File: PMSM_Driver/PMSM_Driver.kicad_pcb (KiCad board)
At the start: 4 copper layers, 244.8 x 144.1 mm, 234 parts, among them J1 1714984, J10 AFBR-2624Z, J11 AFBR-2624Z, J12 AFBR-2624Z, J13 AFBR-2624Z, J14 AFBR-2624Z, J15 AFBR-2624Z, J16 AFBR-2624Z, J17 AFBR-1624Z, J18 AFBR-1624Z, J2 AFBR-2624Z, J3 1714971, J4 1714971, J5 AFBR-1624Z, J6 AFBR-2624Z, J7 AFBR-2624Z, J8 AFBR-2624Z, J9 AFBR-2624Z, Q1 BC846, Q10 BC846, Q11 RGCL60TK60, Q12 RGCL60TK60, Q13 RGCL60TK60, Q14 RGCL60TK60, Q15 BC846, Q16 RGCL60TK60, Q17 RGCL60TK60, Q18 RGCL60TK60, Q19 RGCL60TK60, Q2 BC846, Q20 BC846, Q21 BC846, Q22 BC846, Q23 BC846, Q24 BC846, Q3 BC846, Q4 BC846, Q5 RGCL60TK60, Q6 RGCL60TK60, Q7 RGCL60TK60, Q8 RGCL60TK60, Q9 BC846, U1 74LVC1G04, U10 HCPL-3120, U11 HCPL-3120, U12 HCPL-3120, U13 74LVC1G04, U14 74LVC1G04, U15 74LVC1G04, U16 MGJ2D051515SC, U17 MGJ2D051515SC, U18 MGJ2D051515SC, U19 HCPL-3120, U2 MGJ2D051515SC, U20 HCPL-3120, U21 HCPL-3120, U22 74LVC1G04, U23 74LVC1G04, U24 74LVC1G04, U25 MGJ2D051515SC, U26 MGJ2D051515SC, U27 MGJ2D051515SC, U28 HCPL-3120, U29 HCPL-3120, U3 HCPL-3120, U30 HCPL-3120, U31 74LVC1G04, U32 74LVC1G04, U33 MGJ2D051515SC, U34 MGJ2D051515SC, U35 HCPL-3120, U36 HCPL-3120, U37 VS-E5TH3006S2L-M3, U38 VS-E5TH3006S2L-M3, U39 VS-E5TH3006S2L-M3, U4 74LVC1G04, U40 VS-E5TH3006S2L-M3, U41 VS-E5TH3006S2L-M3, U42 VS-E5TH3006S2L-M3, U43 VS-E5TH3006S2L-M3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

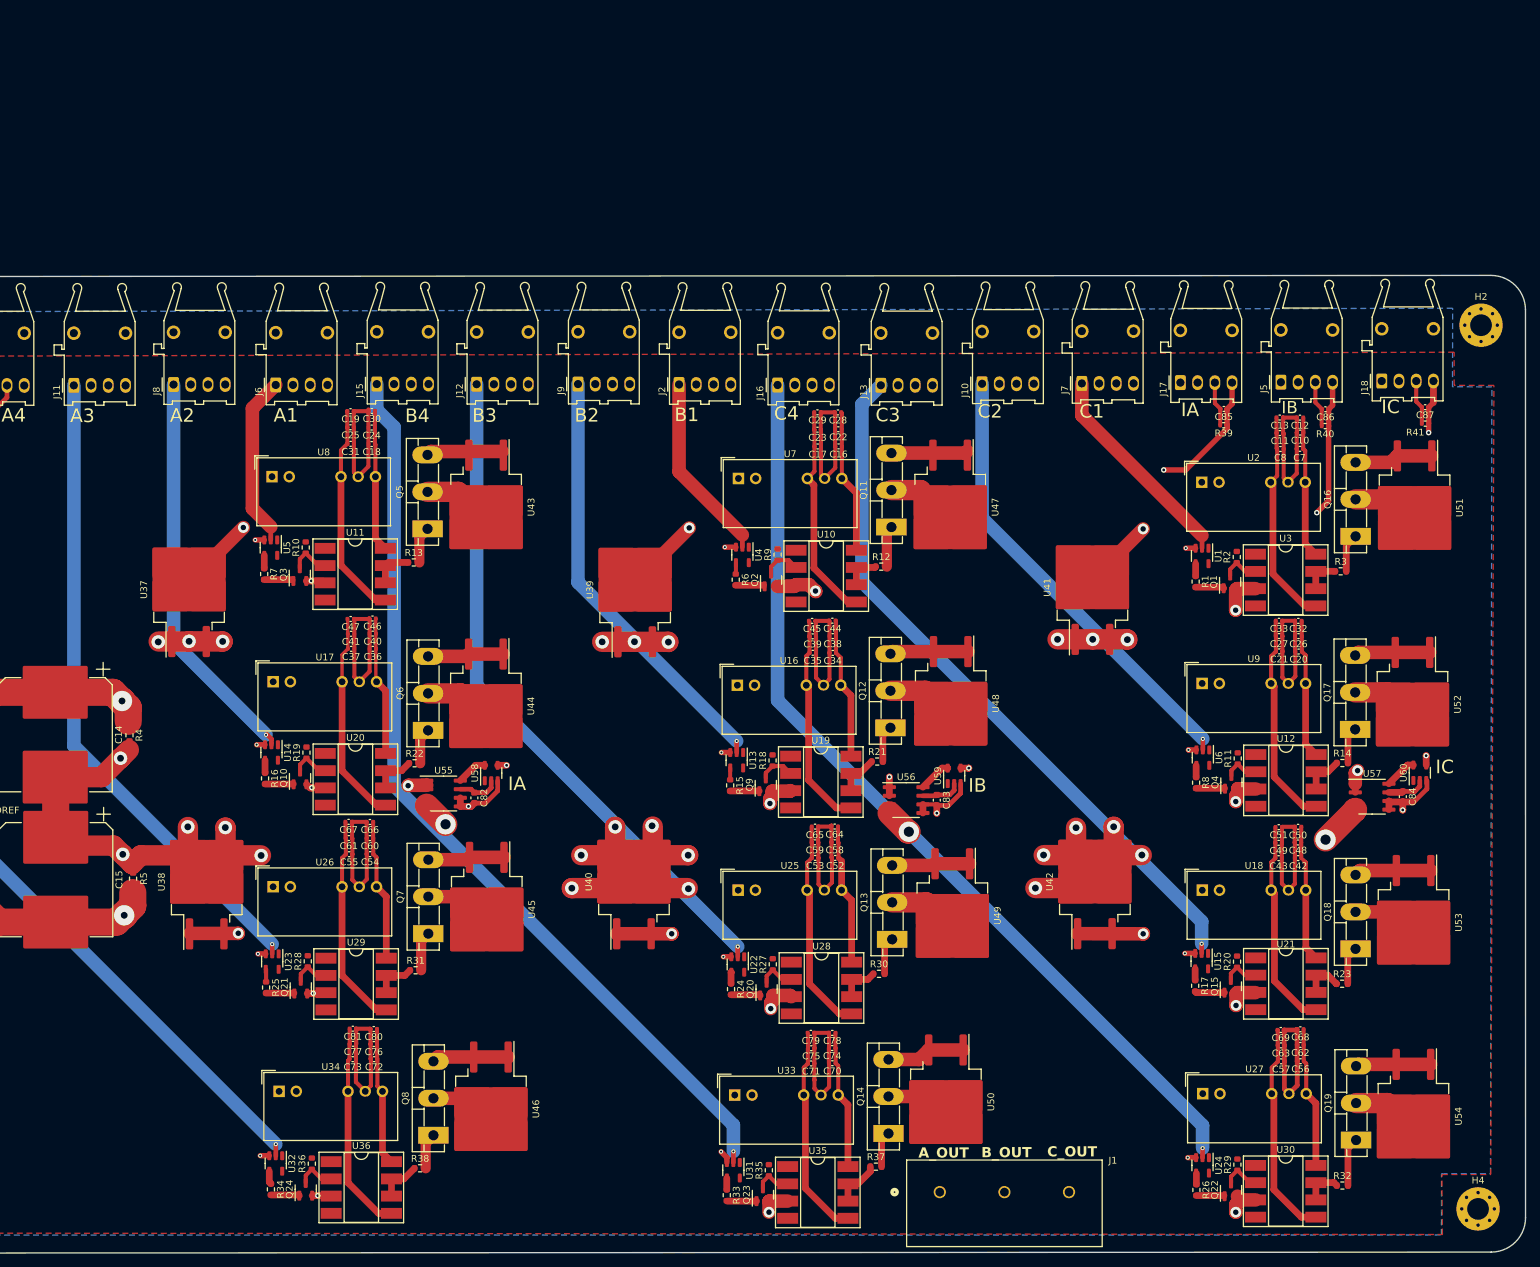
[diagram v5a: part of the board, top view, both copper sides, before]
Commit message: updated PCB layout: gate drive protection
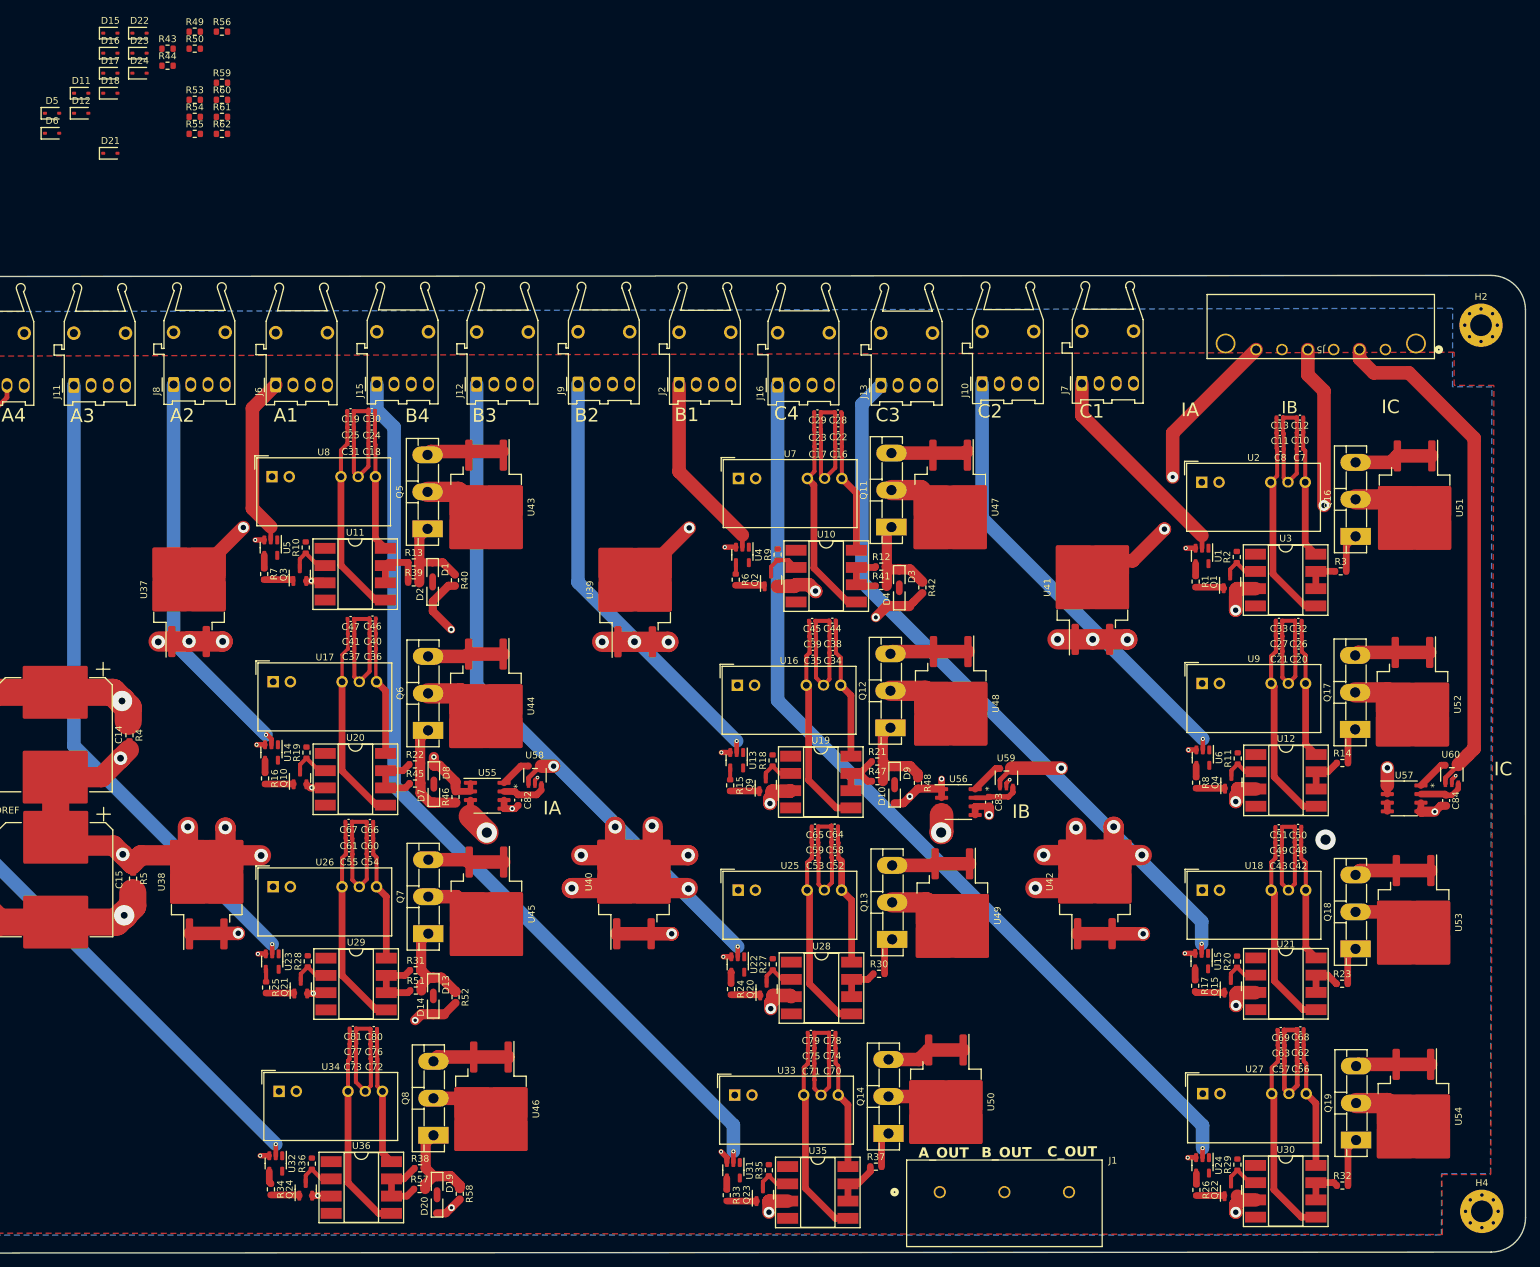
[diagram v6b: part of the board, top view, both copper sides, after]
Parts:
- removed C85, C86, C87: 0.1u, Capacitor_SMD:C_0402_1005Metric
- removed J17, J18: AFBR-1624Z, OptoDevice:Broadcom_AFBR-16xxZ_Horizontal
- added D1: BZX384C18, Diode_SMD:D_SOD-323, F.Cu at (135.7, 81.1)
- added D10: BZX384C18, Diode_SMD:D_SOD-323, F.Cu at (203.8, 114.5)
- added D11: BZX384C18, Diode_SMD:D_SOD-323, F.Cu at (83.9, 11.0)
- added D12: BZX384C18, Diode_SMD:D_SOD-323, F.Cu at (83.9, 13.9)
- added D13: BZX384C18, Diode_SMD:D_SOD-323, F.Cu at (135.8, 142.3)
- added D14: BZX384C18, Diode_SMD:D_SOD-323, F.Cu at (135.8, 145.6)
- added D15: BZX384C18, Diode_SMD:D_SOD-323, F.Cu at (88.2, 2.12)
- added D16: BZX384C18, Diode_SMD:D_SOD-323, F.Cu at (88.2, 5.07)
- added D17: BZX384C18, Diode_SMD:D_SOD-323, F.Cu at (88.2, 8.02)
- added D18: BZX384C18, Diode_SMD:D_SOD-323, F.Cu at (88.2, 11.0)
- added D19: BZX384C18, Diode_SMD:D_SOD-323, F.Cu at (136.4, 171.6)
- added D2: BZX384C18, Diode_SMD:D_SOD-323, F.Cu at (135.7, 84.8)
- added D20: BZX384C18, Diode_SMD:D_SOD-323, F.Cu at (136.3, 175.0)
- added D21: BZX384C18, Diode_SMD:D_SOD-323, F.Cu at (88.2, 19.8)
- added D22: BZX384C18, Diode_SMD:D_SOD-323, F.Cu at (92.5, 2.12)
- added D23: BZX384C18, Diode_SMD:D_SOD-323, F.Cu at (92.5, 5.07)
- added D24: BZX384C18, Diode_SMD:D_SOD-323, F.Cu at (92.5, 8.02)
- added D3: BZX384C18, Diode_SMD:D_SOD-323, F.Cu at (204.5, 82.2)
- added D4: BZX384C18, Diode_SMD:D_SOD-323, F.Cu at (204.5, 85.5)
- added D5: BZX384C18, Diode_SMD:D_SOD-323, F.Cu at (79.6, 13.9)
- added D6: BZX384C18, Diode_SMD:D_SOD-323, F.Cu at (79.6, 16.9)
- added D7: BZX384C18, Diode_SMD:D_SOD-323, F.Cu at (135.9, 114.4)
- added D8: BZX384C18, Diode_SMD:D_SOD-323, F.Cu at (135.9, 111.1)
- added D9: BZX384C18, Diode_SMD:D_SOD-323, F.Cu at (203.8, 111.2)
- added R42: 20k, Resistor_SMD:R_0603_1608Metric, F.Cu at (207.9, 83.8)
- added R43: 50, Resistor_SMD:R_0603_1608Metric, F.Cu at (96.6, 4.41)
- added R44: 20k, Resistor_SMD:R_0603_1608Metric, F.Cu at (96.6, 6.92)
- added R45: 50, Resistor_SMD:R_0603_1608Metric, F.Cu at (133.1, 112.7)
- added R46: 20k, Resistor_SMD:R_0603_1608Metric, F.Cu at (139.1, 114.7)
- added R47: 50, Resistor_SMD:R_0603_1608Metric, F.Cu at (201.2, 112.3)
- added R48: 20k, Resistor_SMD:R_0603_1608Metric, F.Cu at (207.2, 112.6)
- added R49: 50, Resistor_SMD:R_0603_1608Metric, F.Cu at (100.6, 1.90)
- added R50: 20k, Resistor_SMD:R_0603_1608Metric, F.Cu at (100.6, 4.41)
- added R51: 50, Resistor_SMD:R_0603_1608Metric, F.Cu at (133.2, 143.2)
- added R52: 20k, Resistor_SMD:R_0603_1608Metric, F.Cu at (139.1, 144.2)
- added R53: 50, Resistor_SMD:R_0603_1608Metric, F.Cu at (100.6, 11.9)
- added R54: 20k, Resistor_SMD:R_0603_1608Metric, F.Cu at (100.6, 14.4)
- added R55: 50, Resistor_SMD:R_0603_1608Metric, F.Cu at (100.6, 17.0)
- added R56: 20k, Resistor_SMD:R_0603_1608Metric, F.Cu at (104.6, 1.90)
- added R57: 50, Resistor_SMD:R_0603_1608Metric, F.Cu at (133.8, 172.4)
- added R58: 20k, Resistor_SMD:R_0603_1608Metric, F.Cu at (139.7, 173.1)
- added R59: 50, Resistor_SMD:R_0603_1608Metric, F.Cu at (104.6, 9.43)
- added R60: 20k, Resistor_SMD:R_0603_1608Metric, F.Cu at (104.6, 11.9)
- added R61: 50, Resistor_SMD:R_0603_1608Metric, F.Cu at (104.6, 14.4)
- added R62: 20k, Resistor_SMD:R_0603_1608Metric, F.Cu at (104.6, 17.0)
- J5: value AFBR-1624Z -> 1827907; footprint OptoDevice:Broadcom_AFBR-16xxZ_Horizontal -> FYP_Components:CONN_1827907
- R12, R13, R14, R21, R22, R23, R3, R30, R31, R32, R37, R38: value 10 -> 50
- R39, R41: value 4.7k -> 50; footprint Resistor_SMD:R_0402_1005Metric -> Resistor_SMD:R_0603_1608Metric
- R4, R5: value 100M -> 20k
- R40: value 4.7k -> 20k; footprint Resistor_SMD:R_0402_1005Metric -> Resistor_SMD:R_0603_1608Metric
- U58, U59, U60: value SN74LV1T34DBV -> LMV641MF/NOPB; footprint Package_TO_SOT_SMD:SOT-23-5 -> FYP_Components:DBV5_TEX
- moved R40 130.2 mm to (139.0, 82.7), turned to -90 degrees
- moved R39 121.6 mm to (132.9, 83.0), turned to 0 degrees
- moved R41 83.6 mm to (201.8, 83.6), turned to 0 degrees
- moved U59 7.70 mm to (220.2, 111.8)
- moved C83 7.70 mm to (217.7, 115.4)
- moved U56 7.70 mm to (213.2, 115.4)
- moved C82 6.45 mm to (148.3, 115.1)
- moved U55 6.45 mm to (143.7, 114.5)
- moved U58 6.45 mm to (150.8, 111.5)
- moved C84 6.41 mm to (285.0, 115.2)
- moved J5 6.03 mm to (257.0, 48.7), turned to 180 degrees
- moved U60 4.73 mm to (285.9, 111.3)
- moved U57 4.73 mm to (278.8, 114.9)
- moved U45 0.69 mm to (143.6, 131.9)
- moved H4 0.67 mm to (290.3, 175.7)
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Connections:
- J5 pad 1: +5V -> GND
- J5 pad 2: unconnected-(J5-NC-Pad2) -> ic_signal
- J5 pad 8: GND -> (no net)
- R39 pad 1: ia_signal -> Net-(R13-Pad1)
- R39 pad 2: GND -> /A1
- R40 pad 1: ib_signal -> /A1
- R40 pad 2: GND -> /A1_E
- R41 pad 1: ic_signal -> Net-(R12-Pad1)
- R41 pad 2: GND -> /B1
- U58 pad 1: unconnected-(U58-NC-Pad1) -> ia_signal
- U58 pad 2: Net-(U55-VIOUT) -> GND
- U58 pad 3: GND -> Net-(U55-VIOUT)
- U59 pad 1: unconnected-(U59-NC-Pad1) -> ib_signal
- U59 pad 2: Net-(U56-VIOUT) -> GND
- U59 pad 3: GND -> Net-(U56-VIOUT)
- U60 pad 1: unconnected-(U60-NC-Pad1) -> ic_signal
- U60 pad 2: Net-(U57-VIOUT) -> GND
- U60 pad 3: GND -> Net-(U57-VIOUT)
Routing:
- net GND: track 137.1 -> 104.6 mm, vias 27 -> 30
- net /A1_E: track 114.3 -> 134.6 mm, vias 1 -> 2
- net ic_signal: track 57.1 -> 75.7 mm, vias 2 -> 0
- net /A3_E: track 114.9 -> 131.4 mm, vias 1 -> 2
- net /B1_E: track 115.3 -> 130.3 mm, vias 1 -> 2
- net ia_out: track 95.3 -> 106.0 mm
- net /A2: track 5.33 -> 15.4 mm
- net /B2: track 5.44 -> 14.8 mm
- net /B1: track 6.11 -> 15.1 mm
- net /A1: track 5.45 -> 14.4 mm
- net /A4: track 5.34 -> 14.2 mm
- net /A3: track 5.82 -> 14.5 mm
- net ib_out: track 97.1 -> 104.9 mm, vias 1 -> 2
- net c_out: track 86.5 -> 80.2 mm
- net ic_out: track 97.1 -> 101.7 mm
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
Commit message: TBC: change trace for 10A current to filled zone
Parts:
- removed J1: 1714984, FYP_Components:CONN_1714984_PXC
- moved D24 246.8 mm to (272.3, 177.0), turned to 90 degrees
- moved D23 246.4 mm to (272.4, 173.5), turned to -90 degrees
- moved R62 233.0 mm to (275.7, 175.2), turned to -90 degrees
- moved R61 230.1 mm to (269.7, 174.8)
- moved D18 229.1 mm to (272.3, 147.3), turned to 90 degrees
- moved D17 228.9 mm to (272.3, 144.0), turned to -90 degrees
- moved R56 223.2 mm to (275.6, 145.5), turned to -90 degrees
- moved D12 213.7 mm to (272.3, 114.8), turned to 90 degrees
- moved D11 213.5 mm to (272.3, 111.5), turned to -90 degrees
- moved R55 212.1 mm to (269.6, 145.1)
- moved D22 205.1 mm to (203.8, 174.4), turned to 90 degrees
- moved R50 204.9 mm to (275.4, 111.4), turned to -90 degrees
- moved D6 204.5 mm to (272.1, 86.0), turned to 90 degrees
- moved D5 204.4 mm to (272.1, 82.7), turned to -90 degrees
- moved R49 202.1 mm to (269.7, 112.5)
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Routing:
- net a_out: track 105.3 -> 5.79 mm
- net c_out: track 80.2 -> 14.5 mm
- net GNDREF: track 140.7 -> 76.4 mm, vias 25 -> 17
- net b_out: track 60.7 -> 3.88 mm
- net +BATT: track 58.5 -> 19.0 mm, vias 1 -> 37
- net /C3_E: track 117.7 -> 133.3 mm, vias 1 -> 2
- net /B3_E: track 116.2 -> 130.0 mm, vias 1 -> 2
- net /C1_E: track 113.8 -> 127.5 mm, vias 1 -> 2
- net ic_out: track 101.7 -> 113.9 mm
- net /C3: track 5.62 -> 14.6 mm
- net /C4: track 7.20 -> 16.2 mm
- net /B4: track 5.31 -> 14.2 mm
- net /C1: track 5.72 -> 14.6 mm
- net -BATT: track 182.3 -> 191.2 mm, vias 2 -> 4
- net /B3: track 5.54 -> 14.4 mm
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- added copper zone on F.Cu, net +BATT
- added copper zone on F.Cu, net GNDREF
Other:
- board size 244.8 x 144.1 mm -> 261.6 x 144 mm
- board text added: "GND"

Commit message: TBC: filled zone to replece wide trace
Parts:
- added J1: 2606-1101, FYP_Components:CONN_2606-1101_WAG, F.Cu at (167.3, 158.4)
- added J17: 2606-1101, FYP_Components:CONN_2606-1101_WAG, F.Cu at (236.9, 158.6)
- added J18: 2606-1101, FYP_Components:CONN_2606-1101_WAG, F.Cu at (298.1, 158.8)
- moved J5 14.0 mm to (267.6, 51.0)
- moved J7 10.8 mm to (242.1, 53.7)
- moved J10 10.1 mm to (226.8, 53.7)
- moved J13 9.44 mm to (211.2, 53.6)
- moved J16 8.92 mm to (195.4, 53.7)
- moved J2 7.89 mm to (179.9, 53.6)
- moved J9 7.42 mm to (164.5, 53.5)
- moved J12 6.60 mm to (148.8, 53.5)
- moved J15 5.81 mm to (133.3, 53.6)
- moved J6 4.99 mm to (117.6, 53.8)
- moved J8 4.24 mm to (101.8, 53.9)
- moved J11 2.27 mm to (85.1, 54.0)
- moved U45 2.14 mm to (143.5, 134.0)
- moved D24 1.74 mm to (272.3, 175.2)
- moved R32 1.74 mm to (269.7, 170.2)
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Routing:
- net GND: track 105.7 -> 287.5 mm, vias 30 -> 37
- net ib_signal: track 88.5 -> 0.00 mm, vias 2 -> 1
- net -BATT: track 191.2 -> 106.4 mm, vias 4 -> 112
- net ic_signal: track 77.3 -> 0.00 mm
- net GNDREF: track 76.4 -> 0.11 mm, vias 17 -> 123
- net /A1_E: track 134.6 -> 128.4 mm, vias 2 -> 12
- net Net-(J13-Data_Out): track 105.7 -> 99.8 mm
- net a_out: track 5.79 -> 0.00 mm, vias 1 -> 13
- net Net-(J7-Data_Out): track 31.6 -> 27.1 mm
- net ia_out: track 106.0 -> 110.4 mm, vias 1 -> 23
- net /C3_E: track 133.3 -> 137.7 mm
- net Net-(J10-Data_Out): track 67.4 -> 63.3 mm
- net Net-(J16-Data_Out): track 139.8 -> 136.4 mm
- net /A3_E: track 131.4 -> 128.5 mm
- net /B3_E: track 130.0 -> 132.8 mm
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- added copper zone on F.Cu, net -BATT
- added copper zone on F.Cu, net /A1_E
- added copper zone on In1.Cu, net /A1_E
- added copper zone on F.Cu, net GND
- added copper zone on F.Cu, net a_out
- added copper zone on F.Cu, net ia_out
- added copper zone on In1.Cu, net ia_out
- added copper zone on In2.Cu, net ia_out
- added copper zone on F.Cu, net ia_signal
- added copper zone on F.Cu, net ib_signal
- added copper zone on F.Cu, net ic_signal
